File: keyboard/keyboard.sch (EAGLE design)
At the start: 46 parts, among them SW1 CHERRY_MX, SW10 CHERRY_MX, SW11 CHERRY_MX, SW12 CHERRY_MX, SW13 CHERRY_MX, SW14 CHERRY_MX, SW15 CHERRY_MX, SW16 CHERRY_MX, SW17 CHERRY_MX, SW18 CHERRY_MX, SW19 CHERRY_MX, SW2 CHERRY_MX, SW20 CHERRY_MX, SW21 CHERRY_MX, SW22 CHERRY_MX, SW23 CHERRY_MX, SW24 CHERRY_MX, SW25 CHERRY_MX, SW26 CHERRY_MX, SW27 CHERRY_MX, SW28 CHERRY_MX, SW3 CHERRY_MX, SW4 CHERRY_MX, SW5 CHERRY_MX, SW6 CHERRY_MX, SW7 CHERRY_MX, SW8 CHERRY_MX, SW9 CHERRY_MX

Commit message: reroute
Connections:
- new net SW29: U$1.P10, U$6.P30
- net SW10: now also U$1.P30, U$6.P10; no longer U$1.P00, U$6.P13
- net SW12: now also U$6.P13; no longer U$6.P02
- net SW13: now also U$1.P06, U$6.P03; no longer U$1.P07, U$6.P06
- net SW14: now also U$1.P02, U$6.P07; no longer U$1.P03, U$6.P10
- net SW17: now also U$1.P09, U$6.P00; no longer U$1.P10, U$6.P03
- net SW18: now also U$1.P05, U$6.P04; no longer U$1.P06, U$6.P07
- net SW19: now also U$1.P01, U$6.P08; no longer U$1.P02, U$6.P11
- net SW2: now also U$6.P11; no longer U$6.P00
- net SW3: now also U$1.P08, U$6.P01; no longer U$1.P09, U$6.P04
- net SW4: now also U$1.P04, U$6.P05; no longer U$1.P05, U$6.P08
- net SW5: now also U$1.P00, U$6.P09; no longer U$1.P01, U$6.P12
- net SW7: now also U$6.P12; no longer U$6.P01
- net SW8: now also U$1.P07, U$6.P02; no longer U$1.P08, U$6.P05
- net SW9: now also U$1.P03, U$6.P06; no longer U$1.P04, U$6.P09

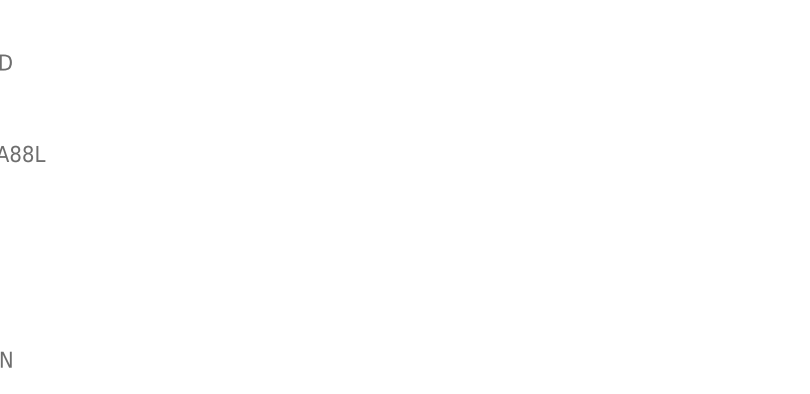
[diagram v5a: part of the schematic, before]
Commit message: add induction charger header
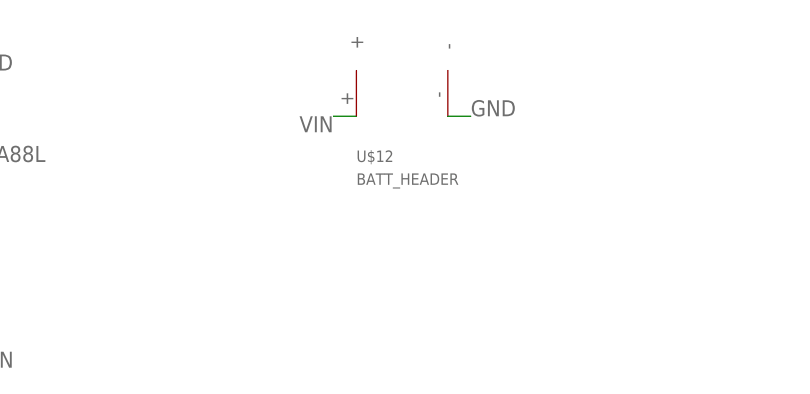
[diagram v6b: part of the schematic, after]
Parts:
- added U$12: BATT_HEADER, batt_header:BATT_HEADER
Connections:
- net GND: now also U$12.-
- net VIN: now also U$12.+
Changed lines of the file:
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@@
 <part name="U$10" library="GRM32ER71H475KA88L" deviceset="GRM32ER71H475KA88L" device=""/>
 <part name="U$11" library="GRM32ER71H475KA88L" deviceset="GRM32ER71H475KA88L" device=""/>
+<part name="U$12" library="batt_header" deviceset="BATT_HEADER" device=""/>
 </parts>
 <sheets>
@@
 <instance part="U$10" gate="G$1" x="337.82" y="66.04"/>
 <instance part="U$11" gate="G$1" x="370.84" y="66.04"/>
+<instance part="U$12" gate="G$1" x="208.28" y="68.58"/>
 </instances>
 <busses>
@@
 <label x="383.54" y="68.58" size="1.778" layer="95"/>
 </segment>
+<segment>
+<pinref part="U$12" gate="G$1" pin="-"/>
+<wire x1="213.36" y1="68.58" x2="215.9" y2="68.58" width="0.1524" layer="91"/>
+<label x="215.9" y="68.58" size="1.778" layer="95"/>
+</segment>
 </net>
 <net name="SW1" class="0">
@@
 <label x="358.14" y="68.58" size="1.778" layer="95"/>
 </segment>
-</net>
+<segment>
+<pinref part="U$12" gate="G$1" pin="+"/>
+<wire x1="203.2" y1="68.58" x2="200.66" y2="68.58" width="0.1524" layer="91"/>
+<label x="200.66" y="68.58" size="1.778" layer="95" rot="R180"/>
+</segment>
+</net>

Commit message: finish routing
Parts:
- removed G1: SL-340/P3.6V, battery:SL-340/P3.6V
- added U$13: BATT_HEADER, batt_header:BATT_HEADER
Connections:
- net GND: now also U$13.-; no longer G1.-
- net VCC: now also U$13.+; no longer G1.+
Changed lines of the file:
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@@
 <part name="SW28" library="cherry_mx" deviceset="CHERRY_MX" device=""/>
 <part name="U$2" library="mcp73831t" deviceset="MCP73831T" device=""/>
-<part name="G1" library="battery" library_urn="urn:adsk.eagle:library:109" deviceset="SL-340/P3.6V" device="" package3d_urn="urn:adsk.eagle:package:4605/1"/>
 <part name="U$6" library="core51822b" deviceset="CORE51822B" device=""/>
 <part name="R2" library="resistor" library_urn="urn:adsk.eagle:library:348" deviceset="R-US_" device="R1210" package3d_urn="urn:adsk.eagle:package:26063/1" value="2k"/>
@@
 <part name="U$11" library="GRM32ER71H475KA88L" deviceset="GRM32ER71H475KA88L" device=""/>
 <part name="U$12" library="batt_header" deviceset="BATT_HEADER" device=""/>
+<part name="U$13" library="batt_header" deviceset="BATT_HEADER" device=""/>
 </parts>
 <sheets>
@@
 <instance part="SW28" gate="G$1" x="243.84" y="-205.74"/>
 <instance part="U$2" gate="G$1" x="45.72" y="33.02"/>
-<instance part="G1" gate="G$1" x="66.04" y="73.66"/>
 <instance part="U$6" gate="G$1" x="256.54" y="-264.16"/>
 <instance part="R2" gate="G$1" x="88.9" y="40.64"/>
@@
 <instance part="U$11" gate="G$1" x="370.84" y="66.04"/>
 <instance part="U$12" gate="G$1" x="208.28" y="68.58"/>
+<instance part="U$13" gate="G$1" x="40.64" y="76.2"/>
 </instances>
 <busses>
@@
 </segment>
 <segment>
-<pinref part="G1" gate="G$1" pin="-"/>
-<wire x1="60.96" y1="73.66" x2="53.34" y2="73.66" width="0.1524" layer="91"/>
-<label x="53.34" y="73.66" size="1.778" layer="95" rot="R180"/>
-</segment>
-<segment>
 <pinref part="U$6" gate="G$1" pin="GND0"/>
 <wire x1="236.22" y1="-248.92" x2="218.44" y2="-248.92" width="0.1524" layer="91"/>
@@
 <wire x1="213.36" y1="68.58" x2="215.9" y2="68.58" width="0.1524" layer="91"/>
 <label x="215.9" y="68.58" size="1.778" layer="95"/>
+</segment>
+<segment>
+<pinref part="U$13" gate="G$1" pin="-"/>
+<wire x1="45.72" y1="76.2" x2="50.8" y2="76.2" width="0.1524" layer="91"/>
+<label x="50.8" y="76.2" size="1.778" layer="95"/>
 </segment>
 </net>
@@
 </segment>
 <segment>
-<pinref part="G1" gate="G$1" pin="+"/>
-<wire x1="71.12" y1="73.66" x2="81.28" y2="73.66" width="0.1524" layer="91"/>
-<label x="81.28" y="73.66" size="1.778" layer="95"/>
-</segment>
-<segment>
 <pinref part="U$6" gate="G$1" pin="VCC"/>
 <wire x1="236.22" y1="-276.86" x2="218.44" y2="-276.86" width="0.1524" layer="91"/>
@@
 <label x="322.58" y="68.58" size="1.778" layer="95"/>
 </segment>
-</net>
+<segment>
+<pinref part="U$13" gate="G$1" pin="+"/>
+<wire x1="35.56" y1="76.2" x2="30.48" y2="76.2" width="0.1524" layer="91"/>
+<label x="30.48" y="76.2" size="1.778" layer="95" rot="R180"/>
+</segment>
+</net>

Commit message: update names
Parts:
- renumbered U$10 to C3, U$11 to C4, U$12 to INDUCTION_CHARGER, U$13 to BATTERY, U$3 to LED1, U$4 to C1, U$7 to C2, U$8 to LED2
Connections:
- net GND: now also R4.2; no longer R3.2
- net GREEN: now also R2.1; no longer R3.1
- net PROG: now also R4.1; no longer R2.1
- net RED: now also R3.1; no longer R4.1
- net RSINK: now also R3.2; no longer R4.2
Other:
- moved on the sheet: R1, R2, R3, R4
